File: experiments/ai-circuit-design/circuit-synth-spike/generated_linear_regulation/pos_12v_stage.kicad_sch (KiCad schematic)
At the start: 9 parts

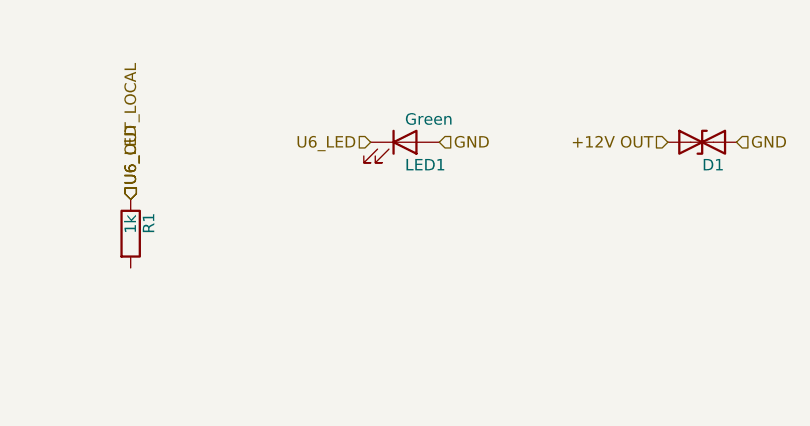
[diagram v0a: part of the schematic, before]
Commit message: fix(experiments): address deep-review findings (SPICE model, LED polarity, skill perms)
Codex review (P2) fixes on the A–D trial artifacts:
- SPICE value-sizing deck: the loop-closed check pinned FB to Vref via an ideal
  source, which floated VOUT (KCL forced VOUT==FB≈1.23V). Replaced with a
  high-gain error-amp behavioral source driving the real divider, so .op now
  genuinely solves VOUT=Vref*(1+Rtop/Rbot). Same fix in the sweep deck; FINDINGS
  method note updated.
- circuit-synth spike: Device:LED pin1=cathode/pin2=anode, but the helper wired
  the positive rail to pin1 → reverse-biased +12V/+5V indicator LEDs. Added a
  rail-aware `negative` flag; positive stages now anode→rail, negative stage
  anode→GND. Regenerated the .kicad_sch/.net/.json output to match.
- pd-schematic-review skill: added `Bash(mkdir -p __inbox*)` to allowed-tools so
  the netlist-export step doesn't block on a fresh clone (__inbox is gitignored).

Co-Authored-By: Claude Opus 4.8 (1M context) <noreply@anthropic.com>
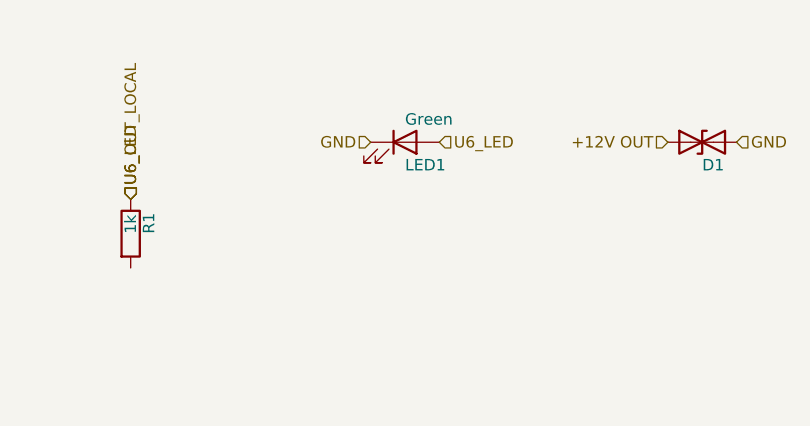
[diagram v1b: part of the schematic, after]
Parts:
- C1, C2, C3, C4, D1, F1, LED1, R1, U6: hierarchy_path /dee5fd78-2d54-41fe-ba07-6c5be7c122e4/a00fa964-fcc6-46ad-ab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 -> /fde22f73-ec7e-4a79-83c1-d101e011a27c/372e7135-437f-4790-bd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; root_uuid dee5fd78-2d54-41fe-ba07-6c5be7c122e4 -> fde22f73-ec7e-4a79-83c1-d101e011a27c
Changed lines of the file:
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@@
 			)
 		)
-		(property "hierarchy_path" "/dee5fd78-2d54-41fe-ba07-6c5be7c122e4/a00fa964-fcc6-46ad-ab97-2272b95a1111"
+		(property "hierarchy_path" "/fde22f73-ec7e-4a79-83c1-d101e011a27c/372e7135-437f-4790-bd67-30e797fb6545"
 			(at 40.64 35.5599 0)
 			(effects
@@
 			)
 		)
-		(property "root_uuid" "dee5fd78-2d54-41fe-ba07-6c5be7c122e4"
+		(property "root_uuid" "fde22f73-ec7e-4a79-83c1-d101e011a27c"
 			(at 40.64 35.5599 0)
 			(effects
@@
 		(instances
 			(project ""
-				(path "/dee5fd78-2d54-41fe-ba07-6c5be7c122e4/a00fa964-fcc6-46ad-ab97-2272b95a1111"
+				(path "/fde22f73-ec7e-4a79-83c1-d101e011a27c/372e7135-437f-4790-bd67-30e797fb6545"
 					(reference "U6")
 					(unit 1)
@@
 			)
 		)
-		(property "hierarchy_path" "/dee5fd78-2d54-41fe-ba07-6c5be7c122e4/a00fa964-fcc6-46ad-ab97-2272b95a1111"
+		(property "hierarchy_path" "/fde22f73-ec7e-4a79-83c1-d101e011a27c/372e7135-437f-4790-bd67-30e797fb6545"
 			(at 187.96 38.0999 0)
 			(effects
@@
 			)
 		)
-		(property "root_uuid" "dee5fd78-2d54-41fe-ba07-6c5be7c122e4"
+		(property "root_uuid" "fde22f73-ec7e-4a79-83c1-d101e011a27c"
 			(at 187.96 38.0999 0)
 			(effects
@@
 		(instances
 			(project ""
-				(path "/dee5fd78-2d54-41fe-ba07-6c5be7c122e4/a00fa964-fcc6-46ad-ab97-2272b95a1111"
+				(path "/fde22f73-ec7e-4a79-83c1-d101e011a27c/372e7135-437f-4790-bd67-30e797fb6545"
 					(reference "C1")
 					(unit 1)
@@
 			)
 		)
-		(property "hierarchy_path" "/dee5fd78-2d54-41fe-ba07-6c5be7c122e4/a00fa964-fcc6-46ad-ab97-2272b95a1111"
+		(property "hierarchy_path" "/fde22f73-ec7e-4a79-83c1-d101e011a27c/372e7135-437f-4790-bd67-30e797fb6545"
 			(at 213.36 38.0999 0)
 			(effects
@@
 			)
 		)
-		(property "root_uuid" "dee5fd78-2d54-41fe-ba07-6c5be7c122e4"
+		(property "root_uuid" "fde22f73-ec7e-4a79-83c1-d101e011a27c"
 			(at 213.36 38.0999 0)
 			(effects
@@
 		(instances
 			(project ""
-				(path "/dee5fd78-2d54-41fe-ba07-6c5be7c122e4/a00fa964-fcc6-46ad-ab97-2272b95a1111"
+				(path "/fde22f73-ec7e-4a79-83c1-d101e011a27c/372e7135-437f-4790-bd67-30e797fb6545"
 					(reference "C2")
 					(unit 1)
@@
 			)
 		)
-		(property "hierarchy_path" "/dee5fd78-2d54-41fe-ba07-6c5be7c122e4/a00fa964-fcc6-46ad-ab97-2272b95a1111"
+		(property "hierarchy_path" "/fde22f73-ec7e-4a79-83c1-d101e011a27c/372e7135-437f-4790-bd67-30e797fb6545"
 			(at 238.76 38.0999 0)
 			(effects
@@
 			)
 		)
-		(property "root_uuid" "dee5fd78-2d54-41fe-ba07-6c5be7c122e4"
+		(property "root_uuid" "fde22f73-ec7e-4a79-83c1-d101e011a27c"
 			(at 238.76 38.0999 0)
 			(effects
@@
 		(instances
 			(project ""
-				(path "/dee5fd78-2d54-41fe-ba07-6c5be7c122e4/a00fa964-fcc6-46ad-ab97-2272b95a1111"
+				(path "/fde22f73-ec7e-4a79-83c1-d101e011a27c/372e7135-437f-4790-bd67-30e797fb6545"
 					(reference "C3")
 					(unit 1)
@@
 			)
 		)
-		(property "hierarchy_path" "/dee5fd78-2d54-41fe-ba07-6c5be7c122e4/a00fa964-fcc6-46ad-ab97-2272b95a1111"
+		(property "hierarchy_path" "/fde22f73-ec7e-4a79-83c1-d101e011a27c/372e7135-437f-4790-bd67-30e797fb6545"
 			(at 264.16 38.0999 0)
 			(effects
@@
 			)
 		)
-		(property "root_uuid" "dee5fd78-2d54-41fe-ba07-6c5be7c122e4"
+		(property "root_uuid" "fde22f73-ec7e-4a79-83c1-d101e011a27c"
 			(at 264.16 38.0999 0)
 			(effects
@@
 		(instances
 			(project ""
-				(path "/dee5fd78-2d54-41fe-ba07-6c5be7c122e4/a00fa964-fcc6-46ad-ab97-2272b95a1111"
+				(path "/fde22f73-ec7e-4a79-83c1-d101e011a27c/372e7135-437f-4790-bd67-30e797fb6545"
 					(reference "C4")
 					(unit 1)
@@
 			)
 		)
-		(property "hierarchy_path" "/dee5fd78-2d54-41fe-ba07-6c5be7c122e4/a00fa964-fcc6-46ad-ab97-2272b95a1111"
+		(property "hierarchy_path" "/fde22f73-ec7e-4a79-83c1-d101e011a27c/372e7135-437f-4790-bd67-30e797fb6545"
 			(at 73.66 40.6399 0)
 			(effects
@@
 			)
 		)
-		(property "root_uuid" "dee5fd78-2d54-41fe-ba07-6c5be7c122e4"
+		(property "root_uuid" "fde22f73-ec7e-4a79-83c1-d101e011a27c"
 			(at 73.66 40.6399 0)
 			(effects
@@
 		(instances
 			(project ""
-				(path "/dee5fd78-2d54-41fe-ba07-6c5be7c122e4/a00fa964-fcc6-46ad-ab97-2272b95a1111"
+				(path "/fde22f73-ec7e-4a79-83c1-d101e011a27c/372e7135-437f-4790-bd67-30e797fb6545"
 					(reference "F1")
 					(unit 1)
@@
 			)
 		)
-		(property "hierarchy_path" "/dee5fd78-2d54-41fe-ba07-6c5be7c122e4/a00fa964-fcc6-46ad-ab97-2272b95a1111"
+		(property "hierarchy_path" "/fde22f73-ec7e-4a79-83c1-d101e011a27c/372e7135-437f-4790-bd67-30e797fb6545"
 			(at 160.02 30.4799 0)
 			(effects
@@
 			)
 		)
-		(property "root_uuid" "dee5fd78-2d54-41fe-ba07-6c5be7c122e4"
+		(property "root_uuid" "fde22f73-ec7e-4a79-83c1-d101e011a27c"
 			(at 160.02 30.4799 0)
 			(effects
@@
 		(instances
 			(project ""
-				(path "/dee5fd78-2d54-41fe-ba07-6c5be7c122e4/a00fa964-fcc6-46ad-ab97-2272b95a1111"
+				(path "/fde22f73-ec7e-4a79-83c1-d101e011a27c/372e7135-437f-4790-bd67-30e797fb6545"
 					(reference "D1")
 					(unit 1)
@@
 			)
 		)
-		(property "hierarchy_path" "/dee5fd78-2d54-41fe-ba07-6c5be7c122e4/a00fa964-fcc6-46ad-ab97-2272b95a1111"
+		(property "hierarchy_path" "/fde22f73-ec7e-4a79-83c1-d101e011a27c/372e7135-437f-4790-bd67-30e797fb6545"
 			(at 96.52 40.6399 0)
 			(effects
@@
 			)
 		)
-		(property "root_uuid" "dee5fd78-2d54-41fe-ba07-6c5be7c122e4"
+		(property "root_uuid" "fde22f73-ec7e-4a79-83c1-d101e011a27c"
 			(at 96.52 40.6399 0)
 			(effects
@@
 		(instances
 			(project ""
-				(path "/dee5fd78-2d54-41fe-ba07-6c5be7c122e4/a00fa964-fcc6-46ad-ab97-2272b95a1111"
+				(path "/fde22f73-ec7e-4a79-83c1-d101e011a27c/372e7135-437f-4790-bd67-30e797fb6545"
 					(reference "R1")
 					(unit 1)
@@
 			)
 		)
-		(property "hierarchy_path" "/dee5fd78-2d54-41fe-ba07-6c5be7c122e4/a00fa964-fcc6-46ad-ab97-2272b95a1111"
+		(property "hierarchy_path" "/fde22f73-ec7e-4a79-83c1-d101e011a27c/372e7135-437f-4790-bd67-30e797fb6545"
 			(at 127 30.4799 0)
 			(effects
@@
 			)
 		)
-		(property "root_uuid" "dee5fd78-2d54-41fe-ba07-6c5be7c122e4"
+		(property "root_uuid" "fde22f73-ec7e-4a79-83c1-d101e011a27c"
 			(at 127 30.4799 0)
 			(effects
@@
 		(instances
 			(project ""
-				(path "/dee5fd78-2d54-41fe-ba07-6c5be7c122e4/a00fa964-fcc6-46ad-ab97-2272b95a1111"
+				(path "/fde22f73-ec7e-4a79-83c1-d101e011a27c/372e7135-437f-4790-bd67-30e797fb6545"
 					(reference "LED1")
 					(unit 1)
@@
 	(hierarchical_label "GND"
 		(shape input)
+		(at 120.65 25.4 180)
+		(effects
+			(font
+				(size 1.27 1.27)
+			)
+			(justify right)
+		)
+	)
+	(hierarchical_label "U6_OUT_LOCAL"
+		(shape input)
+		(at 45.72 30.48 0.0000)
+		(effects
+			(font
+				(size 1.27 1.27)
+			)
+			(justify left)
+		)
+	)
+	(hierarchical_label "U6_OUT_LOCAL"
+		(shape input)
+		(at 45.72 30.48 0.0000)
+		(effects
+			(font
+				(size 1.27 1.27)
+			)
+			(justify left)
+		)
+	)
+	(hierarchical_label "U6_OUT_LOCAL"
+		(shape input)
+		(at 236.22 29.21 90)
+		(effects
+			(font
+				(size 1.27 1.27)
+			)
+			(justify left)
+		)
+	)
+	(hierarchical_label "U6_OUT_LOCAL"
+		(shape input)
+		(at 261.62 29.21 90)
+		(effects
+			(font
+				(size 1.27 1.27)
+			)
+			(justify left)
+		)
+	)
+	(hierarchical_label "U6_OUT_LOCAL"
+		(shape input)
+		(at 71.12 31.75 90)
+		(effects
+			(font
+				(size 1.27 1.27)
+			)
+			(justify left)
+		)
+	)
+	(hierarchical_label "U6_OUT_LOCAL"
+		(shape input)
+		(at 93.98 31.75 90)
+		(effects
+			(font
+				(size 1.27 1.27)
+			)
+			(justify left)
+		)
+	)
+	(hierarchical_label "+12V OUT"
+		(shape input)
+		(at 71.12 31.75 90)
+		(effects
+			(font
+				(size 1.27 1.27)
+			)
+			(justify left)
+		)
+	)
+	(hierarchical_label "+12V OUT"
+		(shape input)
+		(at 153.67 25.4 180)
+		(effects
+			(font
+				(size 1.27 1.27)
+			)
+			(justify right)
+		)
+	)
+	(hierarchical_label "U6_LED"
+		(shape input)
+		(at 93.98 31.75 90)
+		(effects
+			(font
+				(size 1.27 1.27)
+			)
+			(justify left)
+		)
+	)
+	(hierarchical_label "U6_LED"
+		(shape input)
 		(at 128.27 25.4 0.0000)
 		(effects
@@
 		)
 	)
-	(hierarchical_label "U6_OUT_LOCAL"
-		(shape input)
-		(at 45.72 30.48 0.0000)
-		(effects
-			(font
-				(size 1.27 1.27)
-			)
-			(justify left)
-		)
-	)
-	(hierarchical_label "U6_OUT_LOCAL"
-		(shape input)
-		(at 45.72 30.48 0.0000)
-		(effects
-			(font
-				(size 1.27 1.27)
-			)
-			(justify left)
-		)
-	)
-	(hierarchical_label "U6_OUT_LOCAL"
-		(shape input)
-		(at 236.22 29.21 90)
-		(effects
-			(font
-				(size 1.27 1.27)
-			)
-			(justify left)
-		)
-	)
-	(hierarchical_label "U6_OUT_LOCAL"
-		(shape input)
-		(at 261.62 29.21 90)
-		(effects
-			(font
-				(size 1.27 1.27)
-			)
-			(justify left)
-		)
-	)
-	(hierarchical_label "U6_OUT_LOCAL"
-		(shape input)
-		(at 71.12 31.75 90)
-		(effects
-			(font
-				(size 1.27 1.27)
-			)
-			(justify left)
-		)
-	)
-	(hierarchical_label "U6_OUT_LOCAL"
-		(shape input)
-		(at 93.98 31.75 90)
-		(effects
-			(font
-				(size 1.27 1.27)
-			)
-			(justify left)
-		)
-	)
-	(hierarchical_label "+12V OUT"
-		(shape input)
-		(at 71.12 31.75 90)
-		(effects
-			(font
-				(size 1.27 1.27)
-			)
-			(justify left)
-		)
-	)
-	(hierarchical_label "+12V OUT"
-		(shape input)
-		(at 153.67 25.4 180)
-		(effects
-			(font
-				(size 1.27 1.27)
-			)
-			(justify right)
-		)
-	)
-	(hierarchical_label "U6_LED"
-		(shape input)
-		(at 93.98 31.75 90)
-		(effects
-			(font
-				(size 1.27 1.27)
-			)
-			(justify left)
-		)
-	)
-	(hierarchical_label "U6_LED"
-		(shape input)
-		(at 120.65 25.4 180)
-		(effects
-			(font
-				(size 1.27 1.27)
-			)
-			(justify right)
-		)
-	)
